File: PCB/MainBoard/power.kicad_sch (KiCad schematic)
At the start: 13 parts, among them J1 5442170, J2 5442170, J3 5442170, J4 5442170, J8 5442170

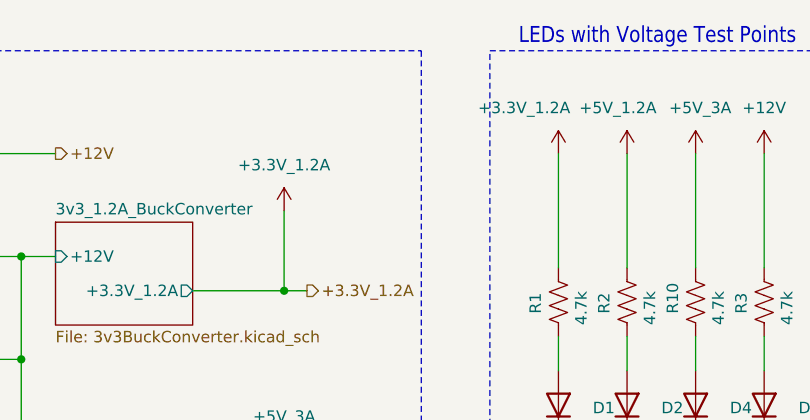
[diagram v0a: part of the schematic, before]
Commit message: adding board v2 progress
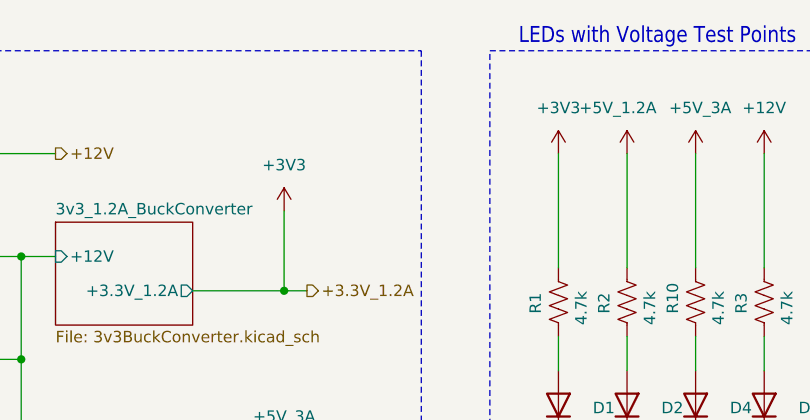
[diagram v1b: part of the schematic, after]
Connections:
- net +3.3V_1.2A renamed +3V3
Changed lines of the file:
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@@
+	)
+	(symbol
+		(lib_id "power:+3V3")
+		(at 184.15 64.77 0)
+		(unit 1)
+		(exclude_from_sim no)
+		(in_bom yes)
+		(on_board yes)
+		(dnp no)
+		(fields_autoplaced yes)
+		(property "Reference" "#PWR07"
+			(at 184.15 68.58 0)
+			(effects
+				(font
+					(size 1.27 1.27)
+				)
+				(hide yes)
+			)
+		)
+		(property "Value" "+3V3"
+			(at 184.15 59.69 0)
+			(effects
+				(font
+					(size 1.27 1.27)
+				)
+			)
+		)
+		(property "Footprint" ""
+			(at 184.15 64.77 0)
+			(effects
+				(font
+					(size 1.27 1.27)
+				)
+				(hide yes)
+			)
+		)
+		(property "Datasheet" ""
+			(at 184.15 64.77 0)
+			(effects
+				(font
+					(size 1.27 1.27)
+				)
+				(hide yes)
+			)
+		)
+		(property "Description" "Power symbol creates a global label with name \"+3V3\""
+			(at 184.15 64.77 0)
+			(effects
+				(font
+					(size 1.27 1.27)
+				)
+				(hide yes)
+			)
+		)
+		(pin "1"
+		)
+		(instances
+			(project "MainBoard"
+				(path "/ce4aa5cc-bc13-46ce-a61c-95c4be48f850/7cb6be40-ad14-404d-82c5-ced68dcd093c"
+					(reference "#PWR07")
+					(unit 1)
+				)
+			)
+		)
 	)
 	(symbol
@@
 	)
 	(symbol
-		(lib_name "+3.3V_1")
-		(lib_id "power:+3.3V")
+		(lib_id "power:+3V3")
 		(at 153.67 71.12 0)
 		(unit 1)
@@
 			)
 		)
-		(property "Value" "+3.3V_1.2A"
+		(property "Value" "+3V3"
 			(at 153.67 66.04 0)
 			(effects
@@
 			)
 		)
-		(property "Description" "Power symbol creates a global label with name \"+3.3V\""
+		(property "Description" "Power symbol creates a global label with name \"+3V3\""
 			(at 153.67 71.12 0)
 			(effects
@@
 					(unit 1)
 				)
-			)
-		)
-	)
-	(symbol
-		(lib_name "+3.3V_1")
-		(lib_id "power:+3.3V")
-		(at 184.15 64.77 0)
-		(unit 1)
-		(exclude_from_sim no)
-		(in_bom yes)
-		(on_board yes)
-		(dnp no)
-		(property "Reference" "#PWR07"
-			(at 184.15 68.58 0)
-			(effects
-				(font
-					(size 1.27 1.27)
-				)
-				(hide yes)
-			)
-		)
-		(property "Value" "+3.3V_1.2A"
-			(at 180.34 59.69 0)
-			(effects
-				(font
-					(size 1.27 1.27)
-				)
-			)
-		)
-		(property "Footprint" ""
-			(at 184.15 64.77 0)
-			(effects
-				(font
-					(size 1.27 1.27)
-				)
-				(hide yes)
-			)
-		)
-		(property "Datasheet" ""
-			(at 184.15 64.77 0)
-			(effects
-				(font
-					(size 1.27 1.27)
-				)
-				(hide yes)
-			)
-		)
-		(property "Description" "Power symbol creates a global label with name \"+3.3V\""
-			(at 184.15 64.77 0)
-			(effects
-				(font
-					(size 1.27 1.27)
-				)
-				(hide yes)
-			)
-		)
-		(pin "1"
-		)
-		(instances
-			(project "MainBoard"
-				(path "/ce4aa5cc-bc13-46ce-a61c-95c4be48f850/7cb6be40-ad14-404d-82c5-ced68dcd093c"
-					(reference "#PWR07")
-					(unit 1)
-				)
